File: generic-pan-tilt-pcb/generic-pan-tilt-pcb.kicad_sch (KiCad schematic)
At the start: 34 parts, among them J1 B4P-VH-FB-B, J10 USB4105-GF-A, J2 NC5MAV, J3 NC5FAV, J4 Conn_01x03, J5 BM03B-SRSS-TBT, J6 Conn_01x03, J7 BM03B-SRSS-TBT, J8 B12B-PH-SM4-TBT, J9 B12B-PH-SM4-TBT, SW1 PTS 647 SK70 SMTR2 LFS, SW2 PTS 647 SK70 SMTR2 LFS

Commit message: fix usb drc errors
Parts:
- J10: footprint USB_C_Receptacle_GCT_USB4105-xx-A_16P_TopMnt_Horizontal -> Connector_USB:USB_C_Receptacle_GCT_USB4105-xx-A_16P_TopMnt_Horizontal
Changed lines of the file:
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@@
 			)
 		)
-		(property "Footprint" "USB_C_Receptacle_GCT_USB4105-xx-A_16P_TopMnt_Horizontal"
+		(property "Footprint" "Connector_USB:USB_C_Receptacle_GCT_USB4105-xx-A_16P_TopMnt_Horizontal"
 			(at 217.17 38.1 0)
 			(effects

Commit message: fix c footprint for r
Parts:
- R1, R2, R3, R4, R5: footprint Capacitor_SMD:C_0402_1005Metric -> Resistor_SMD:R_0402_1005Metric
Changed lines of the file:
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@@
 			)
 		)
-		(property "Footprint" "Capacitor_SMD:C_0402_1005Metric"
+		(property "Footprint" "Resistor_SMD:R_0402_1005Metric"
 			(at 246.126 92.964 90)
 			(effects
@@
 			)
 		)
-		(property "Footprint" "Capacitor_SMD:C_0402_1005Metric"
+		(property "Footprint" "Resistor_SMD:R_0402_1005Metric"
 			(at 221.996 92.964 90)
 			(effects
@@
 			)
 		)
-		(property "Footprint" "Capacitor_SMD:C_0402_1005Metric"
+		(property "Footprint" "Resistor_SMD:R_0402_1005Metric"
 			(at 247.396 35.814 90)
 			(effects
@@
 			)
 		)
-		(property "Footprint" "Capacitor_SMD:C_0402_1005Metric"
+		(property "Footprint" "Resistor_SMD:R_0402_1005Metric"
 			(at 230.124 129.794 90)
 			(effects
@@
 			)
 		)
-		(property "Footprint" "Capacitor_SMD:C_0402_1005Metric"
+		(property "Footprint" "Resistor_SMD:R_0402_1005Metric"
 			(at 255.524 35.306 90)
 			(effects

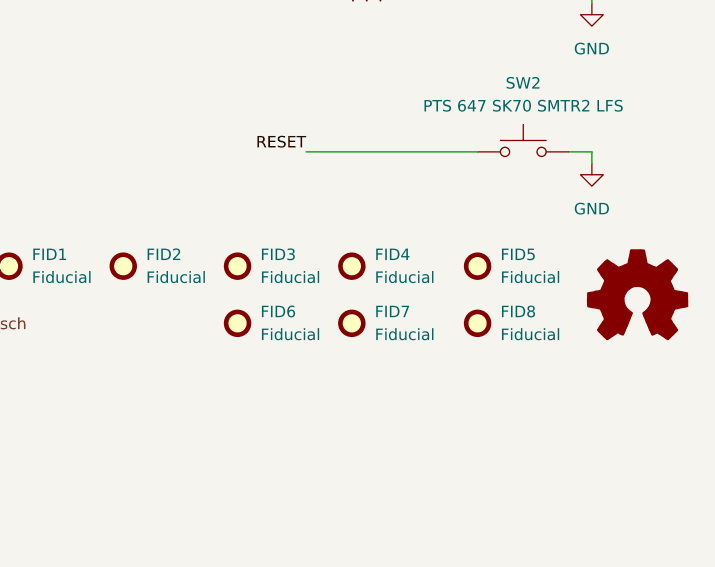
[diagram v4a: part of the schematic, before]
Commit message: 0603 caps for psu rs485
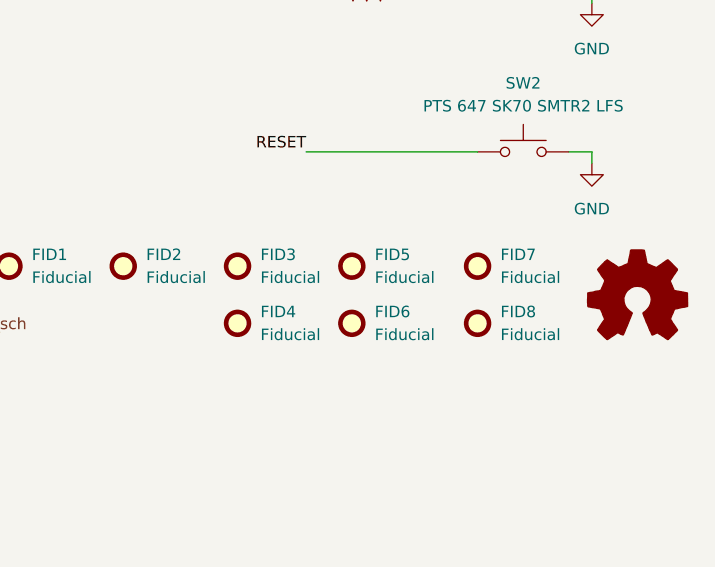
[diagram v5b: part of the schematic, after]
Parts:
- renumbered FID6 to FID4, FID4 to FID5, FID7 to FID6, FID5 to FID7
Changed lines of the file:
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@@
 		(on_board yes)
 		(dnp no)
-		(property "Reference" "FID7"
+		(property "Reference" "FID6"
 			(at 231.14 166.3699 0)
 			(effects
@@
 			(project "generic-pan-tilt-pcb"
 				(path "/e3bbbe58-bf8f-42a8-8505-028de8235dc1"
-					(reference "FID7")
+					(reference "FID6")
 					(unit 1)
 				)
@@
 		(on_board yes)
 		(dnp no)
-		(property "Reference" "FID5"
+		(property "Reference" "FID7"
 			(at 245.11 160.0199 0)
 			(effects
@@
 			(project "generic-pan-tilt-pcb"
 				(path "/e3bbbe58-bf8f-42a8-8505-028de8235dc1"
-					(reference "FID5")
+					(reference "FID7")
 					(unit 1)
 				)
@@
 		(on_board yes)
 		(dnp no)
-		(property "Reference" "FID4"
+		(property "Reference" "FID5"
 			(at 231.14 160.0199 0)
 			(effects
@@
 			(project "generic-pan-tilt-pcb"
 				(path "/e3bbbe58-bf8f-42a8-8505-028de8235dc1"
-					(reference "FID4")
+					(reference "FID5")
 					(unit 1)
 				)
@@
 		(on_board yes)
 		(dnp no)
-		(property "Reference" "FID6"
+		(property "Reference" "FID4"
 			(at 218.44 166.3699 0)
 			(effects
@@
 			(project "generic-pan-tilt-pcb"
 				(path "/e3bbbe58-bf8f-42a8-8505-028de8235dc1"
-					(reference "FID6")
-					(unit 1)
-				)
+					(reference "FID4")
+					(unit 1)
+				)

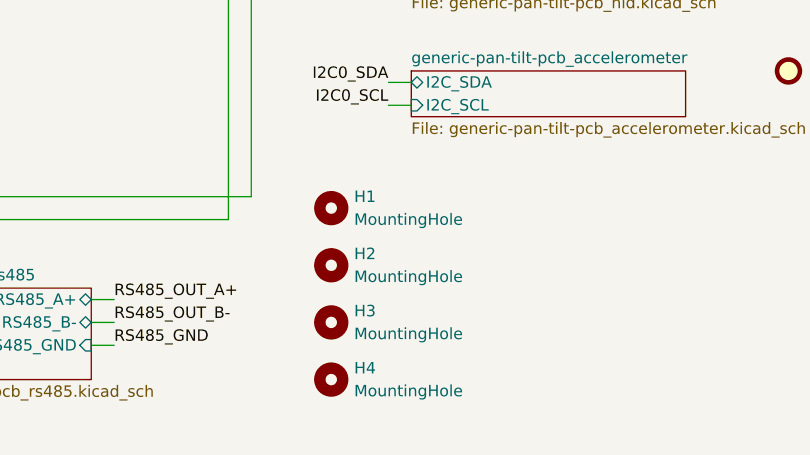
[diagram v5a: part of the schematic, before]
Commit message: move led and dip, add hole
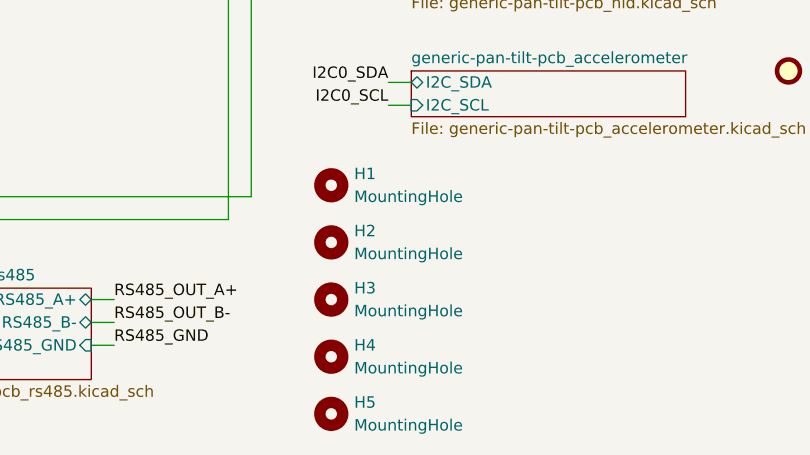
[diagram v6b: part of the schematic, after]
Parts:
- added H5: MountingHole, MountingHole:MountingHole_3.2mm_M3, symbol Mechanical:MountingHole
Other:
- moved on the sheet: H1, H2, H3, H4
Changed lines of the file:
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@@
 	)
 	(symbol
+		(lib_id "Mechanical:MountingHole")
+		(at 139.7 199.39 0)
+		(unit 1)
+		(exclude_from_sim yes)
+		(in_bom no)
+		(on_board yes)
+		(dnp no)
+		(fields_autoplaced yes)
+		(property "Reference" "H5"
+			(at 142.24 198.1199 0)
+			(effects
+				(font
+					(size 1.27 1.27)
+				)
+				(justify left)
+			)
+		)
+		(property "Value" "MountingHole"
+			(at 142.24 200.6599 0)
+			(effects
+				(font
+					(size 1.27 1.27)
+				)
+				(justify left)
+			)
+		)
+		(property "Footprint" "MountingHole:MountingHole_3.2mm_M3"
+			(at 139.7 199.39 0)
+			(effects
+				(font
+					(size 1.27 1.27)
+				)
+				(hide yes)
+			)
+		)
+		(property "Datasheet" "~"
+			(at 139.7 199.39 0)
+			(effects
+				(font
+					(size 1.27 1.27)
+				)
+				(hide yes)
+			)
+		)
+		(property "Description" "Mounting Hole without connection"
+			(at 139.7 199.39 0)
+			(effects
+				(font
+					(size 1.27 1.27)
+				)
+				(hide yes)
+			)
+		)
+		(instances
+			(project "generic-pan-tilt-pcb"
+				(path "/e3bbbe58-bf8f-42a8-8505-028de8235dc1"
+					(reference "H5")
+					(unit 1)
+				)
+			)
+		)
+	)
+	(symbol
 		(lib_id "power:GND")
 		(at 255.27 132.08 0)
@@
 	(symbol
 		(lib_id "Mechanical:MountingHole")
-		(at 139.7 189.23 0)
+		(at 139.7 186.69 0)
 		(unit 1)
 		(exclude_from_sim yes)
@@
 		(fields_autoplaced yes)
 		(property "Reference" "H3"
-			(at 142.24 187.9599 0)
+			(at 142.24 185.4199 0)
 			(effects
 				(font
@@
 		)
 		(property "Value" "MountingHole"
-			(at 142.24 190.4999 0)
+			(at 142.24 187.9599 0)
 			(effects
 				(font
@@
 		)
 		(property "Footprint" "MountingHole:MountingHole_3.2mm_M3"
-			(at 139.7 189.23 0)
+			(at 139.7 186.69 0)
 			(effects
 				(font
@@
 		)
 		(property "Datasheet" "~"
-			(at 139.7 189.23 0)
+			(at 139.7 186.69 0)
 			(effects
 				(font
@@
 		)
 		(property "Description" "Mounting Hole without connection"
-			(at 139.7 189.23 0)
+			(at 139.7 186.69 0)
 			(effects
 				(font
@@
 	(symbol
 		(lib_id "Mechanical:MountingHole")
-		(at 139.7 176.53 0)
+		(at 139.7 173.99 0)
 		(unit 1)
 		(exclude_from_sim yes)
@@
 		(fields_autoplaced yes)
 		(property "Reference" "H1"
-			(at 142.24 175.2599 0)
+			(at 142.24 172.7199 0)
 			(effects
 				(font
@@
 		)
 		(property "Value" "MountingHole"
-			(at 142.24 177.7999 0)
+			(at 142.24 175.2599 0)
 			(effects
 				(font
@@
 		)
 		(property "Footprint" "MountingHole:MountingHole_3.2mm_M3"
-			(at 139.7 176.53 0)
+			(at 139.7 173.99 0)
 			(effects
 				(font
@@
 		)
 		(property "Datasheet" "~"
-			(at 139.7 176.53 0)
+			(at 139.7 173.99 0)
 			(effects
 				(font
@@
 		)
 		(property "Description" "Mounting Hole without connection"
-			(at 139.7 176.53 0)
+			(at 139.7 173.99 0)
 			(effects
 				(font
@@
 	(symbol
 		(lib_id "Mechanical:MountingHole")
-		(at 139.7 195.58 0)
+		(at 139.7 193.04 0)
 		(unit 1)
 		(exclude_from_sim yes)
@@
 		(fields_autoplaced yes)
 		(property "Reference" "H4"
-			(at 142.24 194.3099 0)
+			(at 142.24 191.7699 0)
 			(effects
 				(font
@@
 		)
 		(property "Value" "MountingHole"
-			(at 142.24 196.8499 0)
+			(at 142.24 194.3099 0)
 			(effects
 				(font
@@
 		)
 		(property "Footprint" "MountingHole:MountingHole_3.2mm_M3"
-			(at 139.7 195.58 0)
+			(at 139.7 193.04 0)
 			(effects
 				(font
@@
 		)
 		(property "Datasheet" "~"
-			(at 139.7 195.58 0)
+			(at 139.7 193.04 0)
 			(effects
 				(font
@@
 		)
 		(property "Description" "Mounting Hole without connection"
-			(at 139.7 195.58 0)
+			(at 139.7 193.04 0)
 			(effects
 				(font
@@
 	(symbol
 		(lib_id "Mechanical:MountingHole")
-		(at 139.7 182.88 0)
+		(at 139.7 180.34 0)
 		(unit 1)
 		(exclude_from_sim yes)
@@
 		(fields_autoplaced yes)
 		(property "Reference" "H2"
-			(at 142.24 181.6099 0)
+			(at 142.24 179.0699 0)
 			(effects
 				(font
@@
 		)
 		(property "Value" "MountingHole"
-			(at 142.24 184.1499 0)
+			(at 142.24 181.6099 0)
 			(effects
 				(font
@@
 		)
 		(property "Footprint" "MountingHole:MountingHole_3.2mm_M3"
-			(at 139.7 182.88 0)
+			(at 139.7 180.34 0)
 			(effects
 				(font
@@
 		)
 		(property "Datasheet" "~"
-			(at 139.7 182.88 0)
+			(at 139.7 180.34 0)
 			(effects
 				(font
@@
 		)
 		(property "Description" "Mounting Hole without connection"
-			(at 139.7 182.88 0)
+			(at 139.7 180.34 0)
 			(effects
 				(font

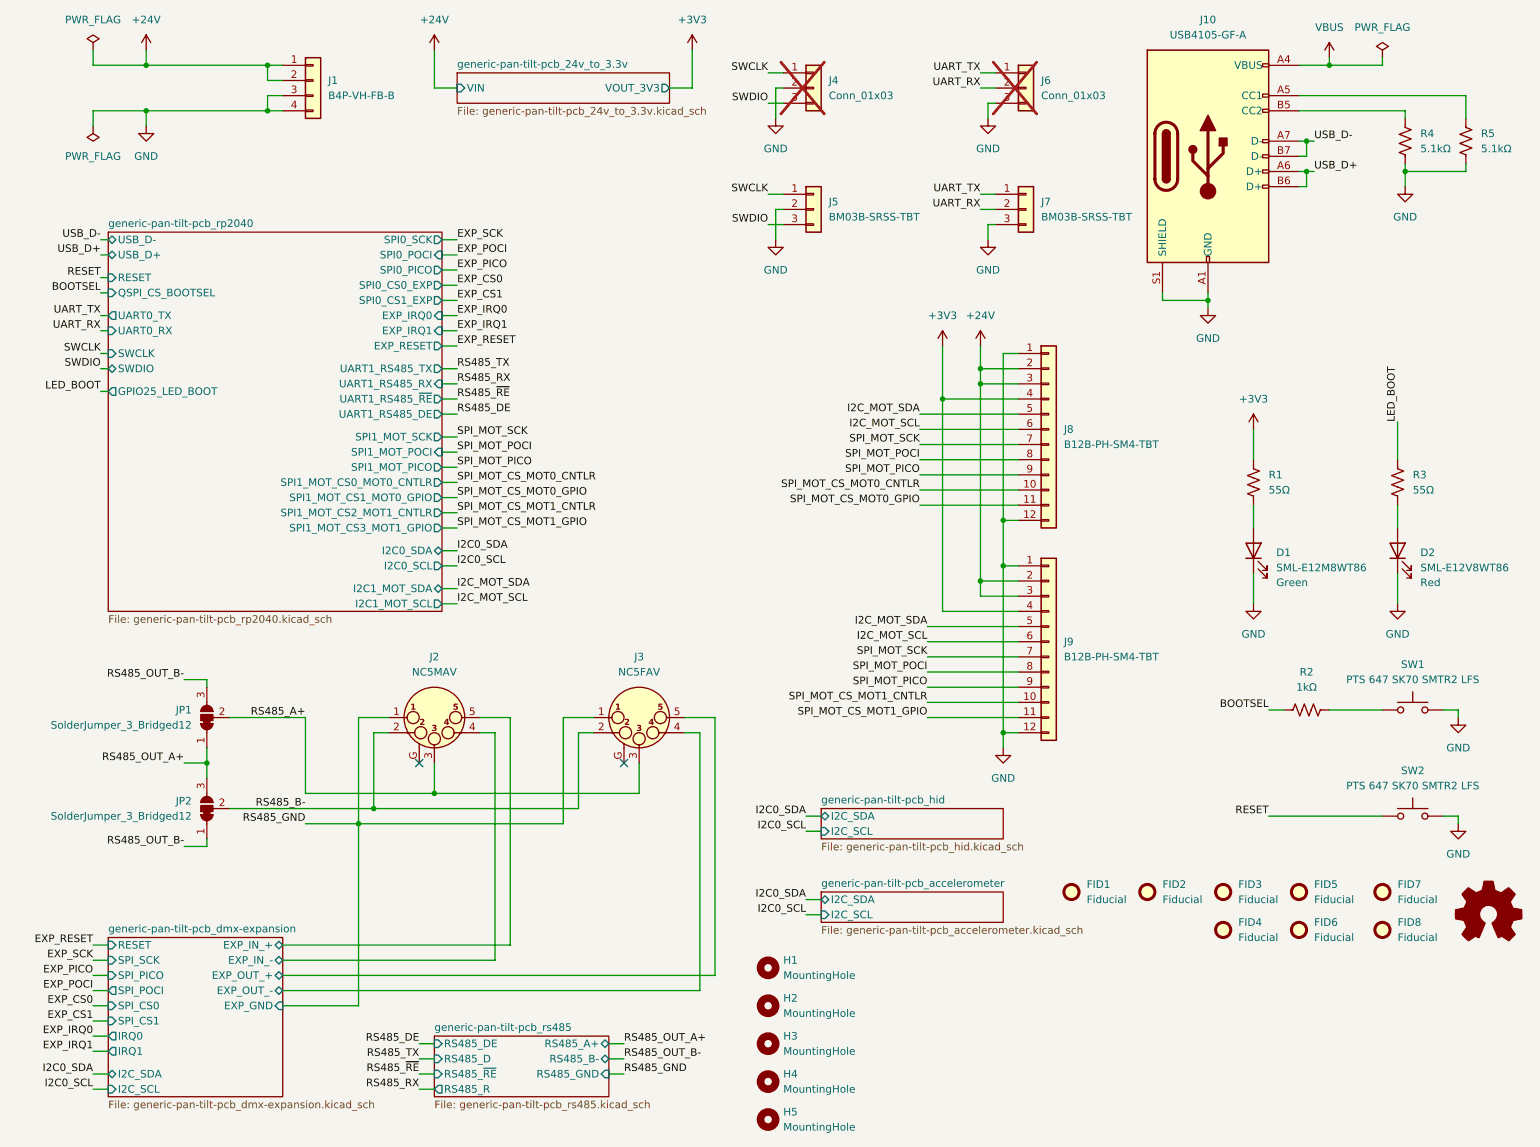
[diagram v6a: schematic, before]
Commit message: fix part numbers, add newark parts, separate fields for part desc
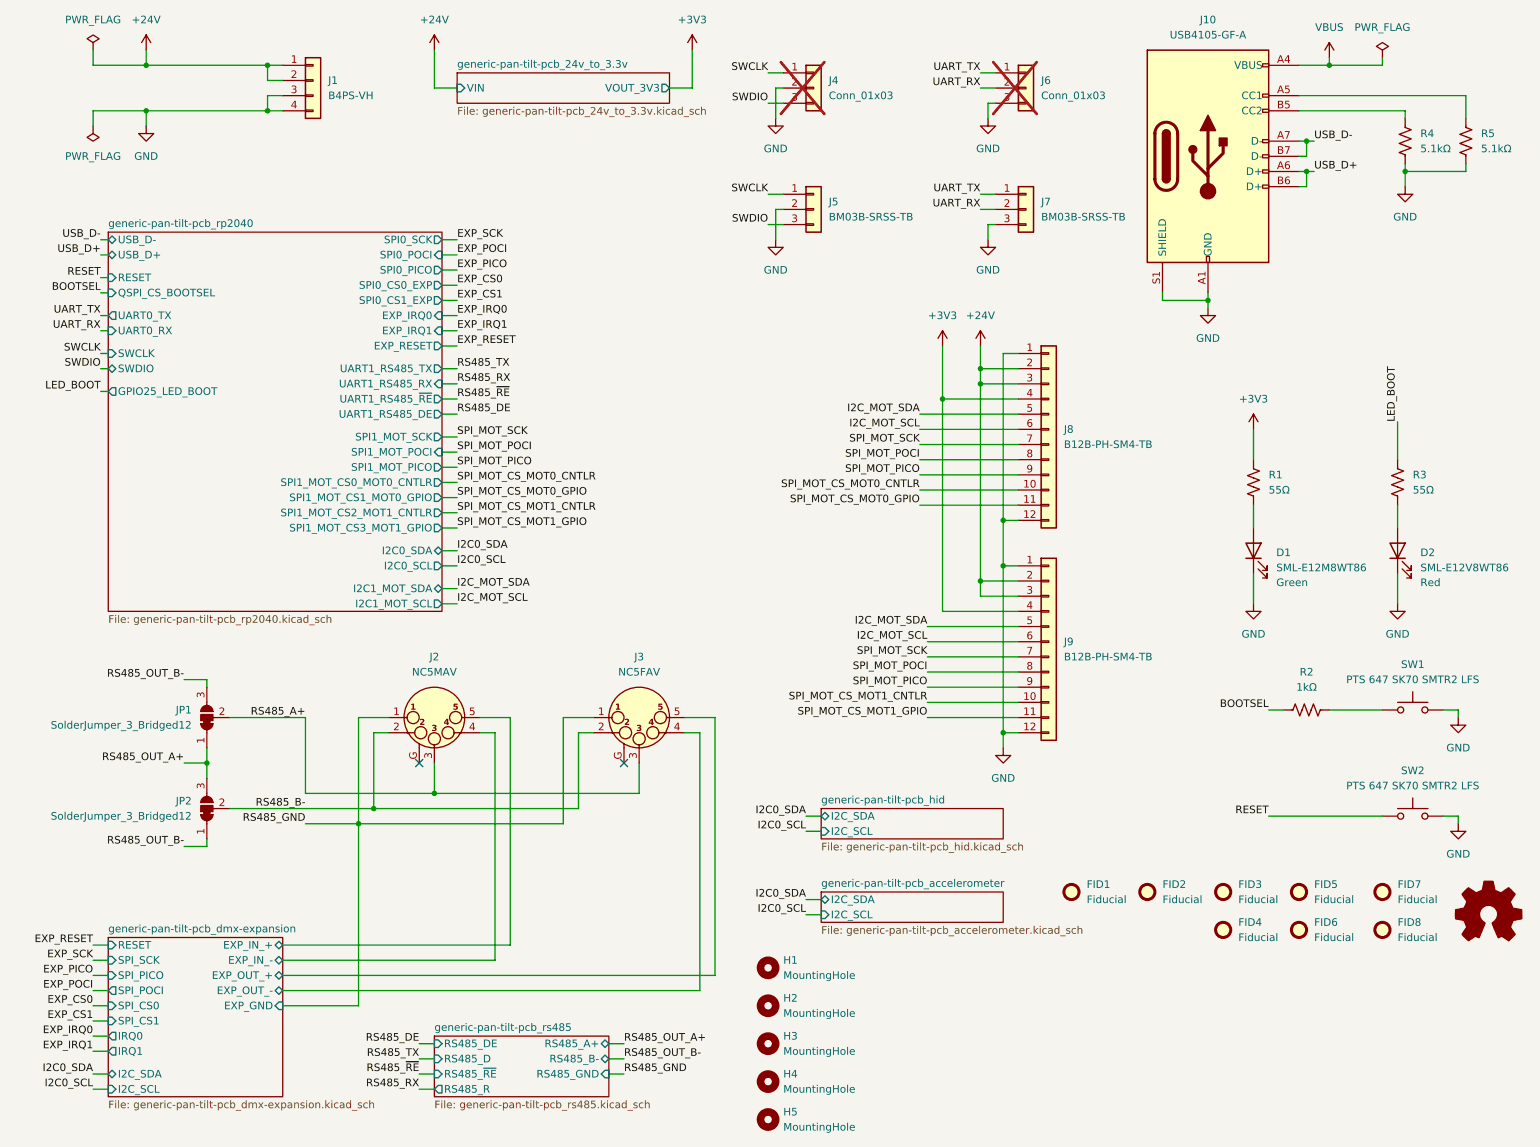
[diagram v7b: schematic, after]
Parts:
- D1: newark# (none) -> 18AC7715
- D2: newark# (none) -> 18AC7719
- J1: value B4P-VH-FB-B -> B4PS-VH; digikey# 455-B4P-VH-FB-B-ND -> 455-B4PS-VH-ND; manf# (none) -> B4PS-VH; newark# (none) -> 37K9965
- J10: newark# (none) -> 86AH2021
- J2: newark# (none) -> 38K6013
- J3: newark# (none) -> 94C1526
- J5, J7: value BM03B-SRSS-TBT -> BM03B-SRSS-TB; digikey# 455-BM03B-SRSS-TBTCT-ND -> 455-BM03B-SRSS-TBCT-ND; manf# (none) -> BM03B-SRSS-TB; newark# (none) -> 33P6549
- J8, J9: value B12B-PH-SM4-TBT -> B12B-PH-SM4-TB; digikey# 455-B12B-PH-SM4-TBTCT-ND -> 455-B12B-PH-SM4-TBCT-ND; manf# (none) -> B12B-PH-SM4-TB; newark# (none) -> 37K9935
- SW1, SW2: newark# (none) -> 03AM1364
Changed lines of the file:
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@@
 			)
 		)
-		(property "Value" "B4P-VH-FB-B"
+		(property "Value" "B4PS-VH"
 			(at 66.04 27.9399 0)
 			(effects
@@
 			)
 		)
-		(property "digikey#" "455-B4P-VH-FB-B-ND"
+		(property "digikey#" "455-B4PS-VH-ND"
+			(at 63.5 25.4 0)
+			(effects
+				(font
+					(size 1.27 1.27)
+				)
+				(hide yes)
+			)
+		)
+		(property "manf#" "B4PS-VH"
+			(at 63.5 25.4 0)
+			(effects
+				(font
+					(size 1.27 1.27)
+				)
+				(hide yes)
+			)
+		)
+		(property "newark#" "37K9965"
 			(at 63.5 25.4 0)
 			(effects
@@
 			)
 		)
-		(property "Value" "B12B-PH-SM4-TBT"
+		(property "Value" "B12B-PH-SM4-TB"
 			(at 189.23 86.3599 0)
 			(effects
@@
 			)
 		)
-		(property "digikey#" "455-B12B-PH-SM4-TBTCT-ND"
+		(property "digikey#" "455-B12B-PH-SM4-TBCT-ND"
+			(at 186.69 83.82 0)
+			(effects
+				(font
+					(size 1.27 1.27)
+				)
+				(hide yes)
+			)
+		)
+		(property "manf#" "B12B-PH-SM4-TB"
+			(at 186.69 83.82 0)
+			(effects
+				(font
+					(size 1.27 1.27)
+				)
+				(hide yes)
+			)
+		)
+		(property "newark#" "37K9935"
 			(at 186.69 83.82 0)
 			(effects
@@
 			)
 		)
-		(property "Value" "BM03B-SRSS-TBT"
+		(property "Value" "BM03B-SRSS-TB"
 			(at 149.86 48.2599 0)
 			(effects
@@
 			)
 		)
-		(property "digikey#" "455-BM03B-SRSS-TBTCT-ND"
+		(property "digikey#" "455-BM03B-SRSS-TBCT-ND"
+			(at 147.32 46.99 0)
+			(effects
+				(font
+					(size 1.27 1.27)
+				)
+				(hide yes)
+			)
+		)
+		(property "manf#" "BM03B-SRSS-TB"
+			(at 147.32 46.99 0)
+			(effects
+				(font
+					(size 1.27 1.27)
+				)
+				(hide yes)
+			)
+		)
+		(property "newark#" "33P6549"
 			(at 147.32 46.99 0)
 			(effects
@@
 			)
 		)
+		(property "newark#" "94C1526"
+			(at 118.11 132.08 0)
+			(effects
+				(font
+					(size 1.27 1.27)
+				)
+				(hide yes)
+			)
+		)
 		(pin "4"
 		)
@@
 			)
 		)
+		(property "newark#" "18AC7719"
+			(at 245.11 104.14 0)
+			(effects
+				(font
+					(size 1.27 1.27)
+				)
+				(hide yes)
+			)
+		)
 		(pin "1"
 		)
@@
 			)
 		)
-		(property "Value" "BM03B-SRSS-TBT"
+		(property "Value" "BM03B-SRSS-TB"
 			(at 185.42 48.2599 0)
 			(effects
@@
 			)
 		)
-		(property "digikey#" "455-BM03B-SRSS-TBTCT-ND"
+		(property "digikey#" "455-BM03B-SRSS-TBCT-ND"
+			(at 182.88 46.99 0)
+			(effects
+				(font
+					(size 1.27 1.27)
+				)
+				(hide yes)
+			)
+		)
+		(property "manf#" "BM03B-SRSS-TB"
+			(at 182.88 46.99 0)
+			(effects
+				(font
+					(size 1.27 1.27)
+				)
+				(hide yes)
+			)
+		)
+		(property "newark#" "33P6549"
 			(at 182.88 46.99 0)
 			(effects
@@
 			)
 		)
+		(property "newark#" "38K6013"
+			(at 83.82 132.08 0)
+			(effects
+				(font
+					(size 1.27 1.27)
+				)
+				(hide yes)
+			)
+		)
 		(pin "3"
 		)
@@
 			)
 		)
+		(property "newark#" "86AH2021"
+			(at 213.36 38.1 0)
+			(effects
+				(font
+					(size 1.27 1.27)
+				)
+				(hide yes)
+			)
+		)
 		(pin "B4"
 		)
@@
 			)
 		)
-		(property "Value" "B12B-PH-SM4-TBT"
+		(property "Value" "B12B-PH-SM4-TB"
 			(at 189.23 121.9199 0)
 			(effects
@@
 			)
 		)
-		(property "digikey#" "455-B12B-PH-SM4-TBTCT-ND"
+		(property "digikey#" "455-B12B-PH-SM4-TBCT-ND"
+			(at 186.69 119.38 0)
+			(effects
+				(font
+					(size 1.27 1.27)
+				)
+				(hide yes)
+			)
+		)
+		(property "manf#" "B12B-PH-SM4-TB"
+			(at 186.69 119.38 0)
+			(effects
+				(font
+					(size 1.27 1.27)
+				)
+				(hide yes)
+			)
+		)
+		(property "newark#" "37K9935"
 			(at 186.69 119.38 0)
 			(effects
@@
 			)
 		)
+		(property "newark#" "03AM1364"
+			(at 247.65 148.59 0)
+			(effects
+				(font
+					(size 1.27 1.27)
+				)
+				(hide yes)
+			)
+		)
 		(pin "1"
 		)
@@
 			)
 		)
+		(property "newark#" "03AM1364"
+			(at 247.65 130.81 0)
+			(effects
+				(font
+					(size 1.27 1.27)
+				)
+				(hide yes)
+			)
+		)
 		(pin "2"
 		)
@@
 			(at 220.98 104.14 0)
 			(effects
+				(font
+					(size 1.27 1.27)
+				)
+				(hide yes)
+			)
+		)
+		(property "newark#" "18AC7715"
+			(at 220.98 104.14 0)
+			(effects
